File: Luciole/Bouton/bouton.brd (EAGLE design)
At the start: 31.8 x 43.8 mm, 28 parts, among them J1 LiPo, J2 USB-MICROB, J3 LED, Q1 2.5A/30V, Q2 MOSFET-NCHANNELAO3404A, U1 MCP73831, U2 3.3V

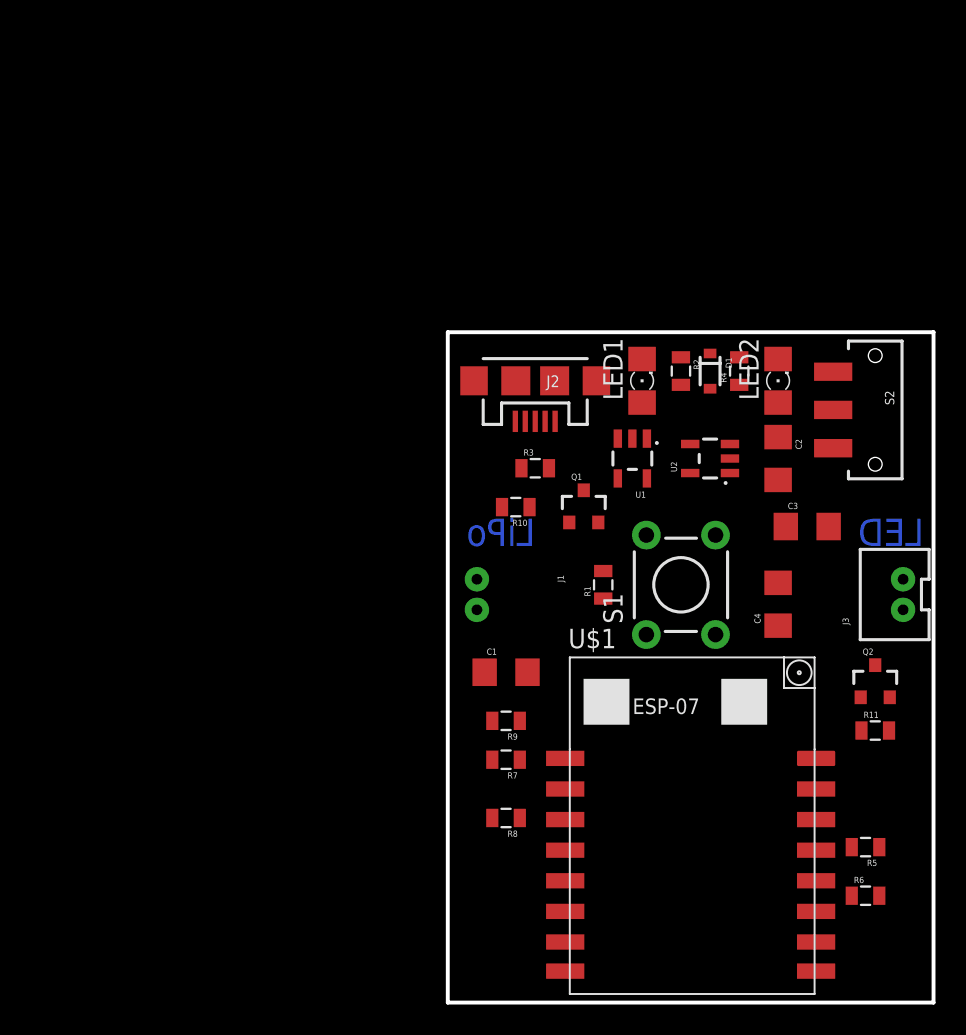
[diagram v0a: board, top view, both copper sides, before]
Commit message: Luciole V1 Ok ; Baballe V1 En cours
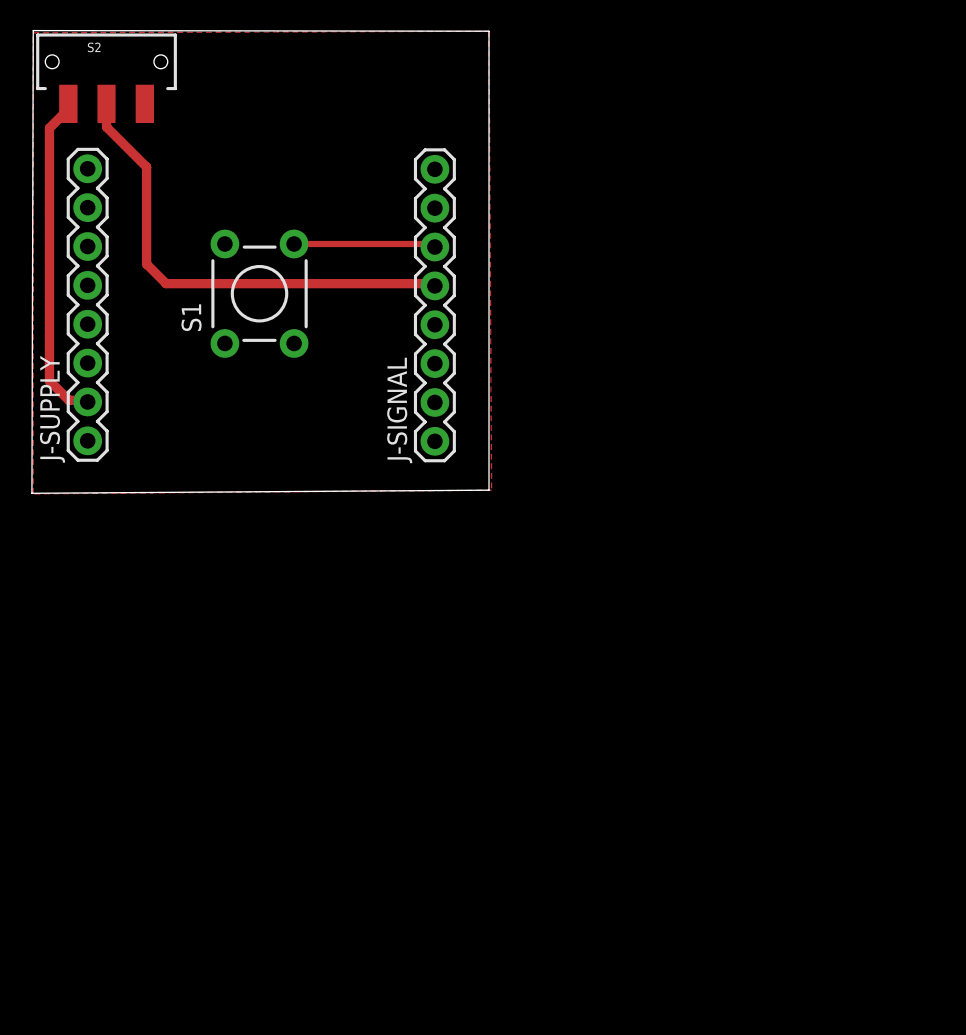
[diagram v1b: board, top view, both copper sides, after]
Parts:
- removed C1: 4.7 uF, SparkFun-Capacitors:1206
- removed C2: 1 uF, SparkFun-Capacitors:1206
- removed C3: 2.2 uF, SparkFun-Capacitors:1206
- removed C4: 100 nF, SparkFun-Capacitors:1206
- removed D1: BAT20J, SparkFun-DiscreteSemi:SOD-323
- removed J1: LiPo, SparkFun-Connectors:JST-2-PTH-NS
- removed J2: USB-MICROB, SparkFun-Connectors:USB-MICROB
- removed J3: LED, SparkFun-Connectors:JST-2-PTH-VERT
- removed LED1: JAUNE, eagle-ltspice:LED_1206
- removed LED2: ROUGE, eagle-ltspice:LED_1206
- removed Q1: 2.5A/30V, SparkFun-DiscreteSemi:SOT23-3
- removed Q2: MOSFET-NCHANNELAO3404A, SparkFun-DiscreteSemi:SOT23-3
- removed R1: 2K, SparkFun-Passives:0805
- removed R10, R11, R3, R5, R6, R7, R8, R9: 10K, SparkFun-Passives:0805
- removed R2: ?, SparkFun-Passives:0805
- removed R4: 200, SparkFun-Passives:0805
- removed U$1: ESP07-16PIN, esp8266modules:ESP07-16PIN
- removed U1: MCP73831, SparkFun-PowerIC:SOT23-5
- removed U2: 3.3V, SparkFun-PowerIC:SOT23-5
- added J-SIGNAL: J-SIGNAL, SparkFun-Connectors:1X08_ROUND
- added J-SUPPLY: J-SUPPLY, SparkFun-Connectors:1X08_ROUND
- S1: value PUSH -> SWITCH-MOMENTARY-2MOT; device SparkFun-Retired:TACTILE-PTH -> SparkFun-Electromechanical:TACTILE-PTH
- S2: value ON / OFF -> (none)
- moved S2 55.2 mm to (5.00, 78.0), turned to 0 degrees
- moved S1 33.5 mm to (15.0, 62.8)
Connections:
- removed net N$1: R5.2, U$1.GPIO15
- removed net N$10: R8.1, U$1.CH_PD
- removed net N$11: R10.2, R9.1, U$1.ADC
- removed net N$12: S1.3, S1.4, U$1.GPIO13
- removed net N$13: Q2.1, R11.1, U$1.GPIO14
- removed net N$14: J3.2, Q2.3
- removed net N$2: R1.2, U1.5
- removed net N$3: S2.2, U2.3
- removed net N$4: R2.2, U1.1
- removed net N$5: LED1.C, R2.1
- removed net N$6: R6.1, U$1.GPIO0
- removed net N$8: LED2.C, R4.2
- removed net N$9: R7.1, U$1.REST
- removed net VUSB: D1.A, J2.VBUS, LED1.A, Q1.1, R3.2, U1.4
- removed net V_BATT: C1.1, J1.1, Q1.3, R10.1, U1.3
- new net ENABLE: J-SIGNAL.5, S2.2
- new net GPIO12: J-SIGNAL.3
- new net GPIO13: J-SIGNAL.2
- new net GPIO14: J-SIGNAL.4
- new net SBUTTON: J-SIGNAL.6, S1.4
- new net SLED: J-SIGNAL.7
- new net VBAT: J-SUPPLY.4
- new net VBAT_MESURE: J-SUPPLY.3
- net GND: now also J-SIGNAL.1, J-SUPPLY.1; no longer C1.2, C2.2, C3.2, C4.1, J1.2, J2.GND, J2.MT1, J2.MT2, Q2.2, R1.1, R11.2, R3.1, R4.1, R5.1, R9.2, S1.2, U$1.GND, U1.2, U2.2, U2.4
- net VCC: now also J-SUPPLY.5; no longer C3.1, C4.2, LED2.A, R6.2, R7.2, R8.2, U$1.GPIO2, U$1.VCC, U2.5
- net VIN: now also J-SUPPLY.2; no longer C2.1, D1.C, J3.1, Q1.2, U2.1
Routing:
- net ENABLE: track 0.00 -> 31.0 mm
- net VIN: track 0.00 -> 21.7 mm
- net SBUTTON: track 0.00 -> 9.40 mm
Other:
- board size 31.8 x 43.8 mm -> 29.9 x 30.2 mm
- board text removed: "LED"
- board text removed: "LiPo"
